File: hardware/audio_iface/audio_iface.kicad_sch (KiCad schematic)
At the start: 0 parts

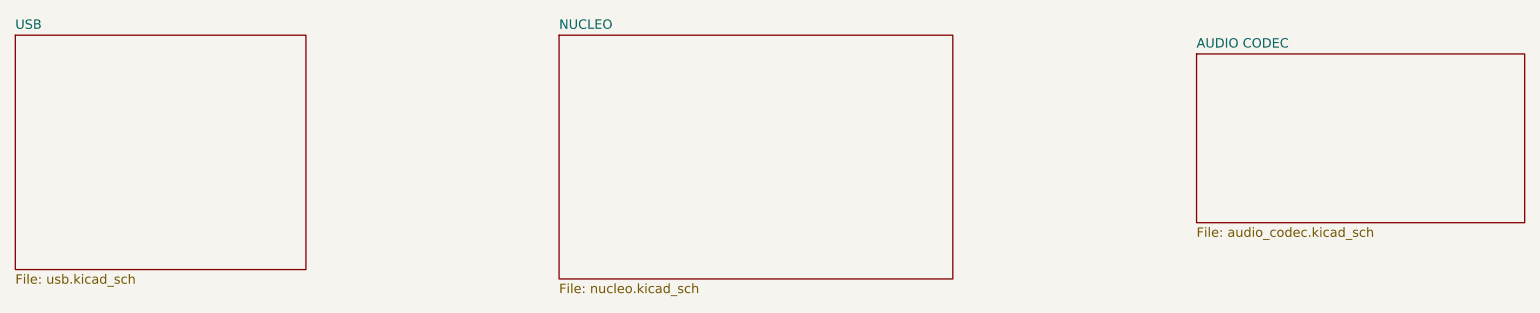
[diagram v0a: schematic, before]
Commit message: added some connections
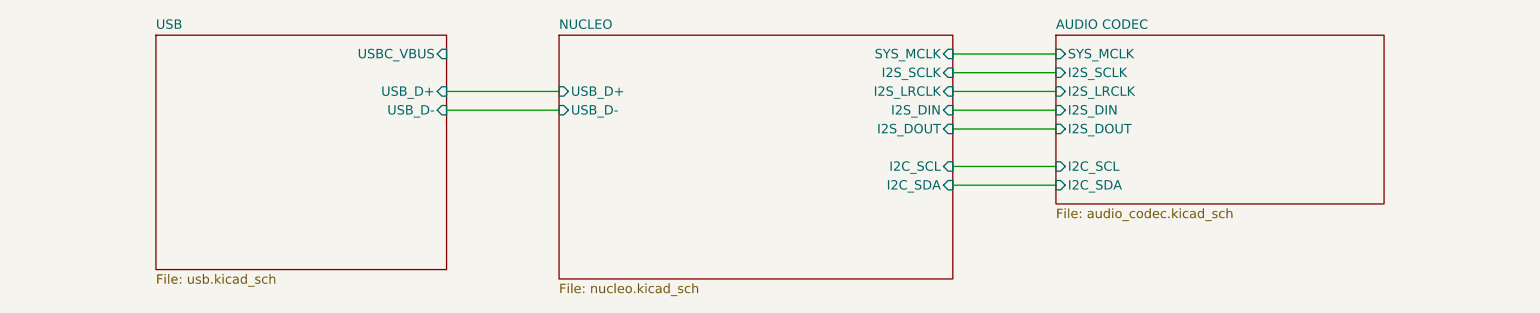
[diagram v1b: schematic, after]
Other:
- sheet AUDIO CODEC ports: added I2C_SCL, I2C_SDA, I2S_DIN, I2S_DOUT, I2S_LRCLK, I2S_SCLK, SYS_MCLK; removed none
- sheet NUCLEO ports: added I2C_SCL, I2C_SDA, I2S_DIN, I2S_DOUT, I2S_LRCLK, I2S_SCLK, SYS_MCLK, USB_D+, USB_D-; removed none
- sheet USB ports: added USBC_VBUS, USB_D+, USB_D-; removed none
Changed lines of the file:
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@@
 (kicad_sch (version 20230121) (generator eeschema)
   (paper "A4")
-  (sheet (at 193.04 59.69) (size 44.45 22.86) (fields_autoplaced)
+  (wire (pts (xy 160.02 62.23) (xy 173.99 62.23))
+    (stroke (width 0) (type default))
+  )
+  (wire (pts (xy 160.02 77.47) (xy 173.99 77.47))
+    (stroke (width 0) (type default))
+  )
+  (wire (pts (xy 160.02 64.77) (xy 173.99 64.77))
+    (stroke (width 0) (type default))
+  )
+  (wire (pts (xy 160.02 59.69) (xy 173.99 59.69))
+    (stroke (width 0) (type default))
+  )
+  (wire (pts (xy 91.44 67.31) (xy 106.68 67.31))
+    (stroke (width 0) (type default))
+  )
+  (wire (pts (xy 160.02 67.31) (xy 173.99 67.31))
+    (stroke (width 0) (type default))
+  )
+  (wire (pts (xy 160.02 69.85) (xy 173.99 69.85))
+    (stroke (width 0) (type default))
+  )
+  (wire (pts (xy 91.44 64.77) (xy 106.68 64.77))
+    (stroke (width 0) (type default))
+  )
+  (wire (pts (xy 160.02 74.93) (xy 173.99 74.93))
+    (stroke (width 0) (type default))
+  )
+  (sheet (at 173.99 57.15) (size 44.45 22.86) (fields_autoplaced)
     (stroke (width 0.1524) (type solid))
     (fill (color 0 0 0 0.0000))
-    (property "Sheetname" "AUDIO CODEC" (at 193.04 58.9784 0)
+    (property "Sheetname" "AUDIO CODEC" (at 173.99 56.4384 0)
       (effects (font (size 1.27 1.27)) (justify left bottom))
     )
-    (property "Sheetfile" "audio_codec.kicad_sch" (at 193.04 83.1346 0)
+    (property "Sheetfile" "audio_codec.kicad_sch" (at 173.99 80.5946 0)
       (effects (font (size 1.27 1.27)) (justify left top))
     )
-    (property "Field2" "" (at 193.04 59.69 0)
+    (property "Field2" "" (at 173.99 57.15 0)
       (effects (font (size 1.27 1.27)) hide)
+    )
+    (pin "I2S_LRCLK" input (at 173.99 64.77 180)
+      (effects (font (size 1.27 1.27)) (justify left))
+    )
+    (pin "I2S_DOUT" input (at 173.99 69.85 180)
+      (effects (font (size 1.27 1.27)) (justify left))
+    )
+    (pin "I2S_SCLK" input (at 173.99 62.23 180)
+      (effects (font (size 1.27 1.27)) (justify left))
+    )
+    (pin "I2S_DIN" input (at 173.99 67.31 180)
+      (effects (font (size 1.27 1.27)) (justify left))
+    )
+    (pin "SYS_MCLK" input (at 173.99 59.69 180)
+      (effects (font (size 1.27 1.27)) (justify left))
+    )
+    (pin "I2C_SDA" input (at 173.99 77.47 180)
+      (effects (font (size 1.27 1.27)) (justify left))
+    )
+    (pin "I2C_SCL" input (at 173.99 74.93 180)
+      (effects (font (size 1.27 1.27)) (justify left))
     )
     (instances
@@
       (effects (font (size 1.27 1.27)) hide)
     )
+    (pin "I2S_LRCLK" input (at 160.02 64.77 0)
+      (effects (font (size 1.27 1.27)) (justify right))
+    )
+    (pin "SYS_MCLK" input (at 160.02 59.69 0)
+      (effects (font (size 1.27 1.27)) (justify right))
+    )
+    (pin "I2S_DOUT" input (at 160.02 69.85 0)
+      (effects (font (size 1.27 1.27)) (justify right))
+    )
+    (pin "I2S_SCLK" input (at 160.02 62.23 0)
+      (effects (font (size 1.27 1.27)) (justify right))
+    )
+    (pin "I2S_DIN" input (at 160.02 67.31 0)
+      (effects (font (size 1.27 1.27)) (justify right))
+    )
+    (pin "I2C_SDA" input (at 160.02 77.47 0)
+      (effects (font (size 1.27 1.27)) (justify right))
+    )
+    (pin "USB_D+" input (at 106.68 64.77 180)
+      (effects (font (size 1.27 1.27)) (justify left))
+    )
+    (pin "USB_D-" input (at 106.68 67.31 180)
+      (effects (font (size 1.27 1.27)) (justify left))
+    )
+    (pin "I2C_SCL" input (at 160.02 74.93 0)
+      (effects (font (size 1.27 1.27)) (justify right))
+    )
     (instances
       (project "audio_iface"
@@
     )
   )
-  (sheet (at 33.02 57.15) (size 39.37 31.75) (fields_autoplaced)
+  (sheet (at 52.07 57.15) (size 39.37 31.75) (fields_autoplaced)
     (stroke (width 0.1524) (type solid))
     (fill (color 0 0 0 0.0000))
-    (property "Sheetname" "USB" (at 33.02 56.4384 0)
+    (property "Sheetname" "USB" (at 52.07 56.4384 0)
       (effects (font (size 1.27 1.27)) (justify left bottom))
     )
-    (property "Sheetfile" "usb.kicad_sch" (at 33.02 89.4846 0)
+    (property "Sheetfile" "usb.kicad_sch" (at 52.07 89.4846 0)
       (effects (font (size 1.27 1.27)) (justify left top))
     )
-    (property "Field2" "" (at 33.02 57.15 0)
+    (property "Field2" "" (at 52.07 57.15 0)
       (effects (font (size 1.27 1.27)) hide)
     )
+    (pin "USBC_VBUS" input (at 91.44 59.69 0)
+      (effects (font (size 1.27 1.27)) (justify right))
+    )
+    (pin "USB_D+" input (at 91.44 64.77 0)
+      (effects (font (size 1.27 1.27)) (justify right))
+    )
+    (pin "USB_D-" input (at 91.44 67.31 0)
+      (effects (font (size 1.27 1.27)) (justify right))
+    )
     (instances

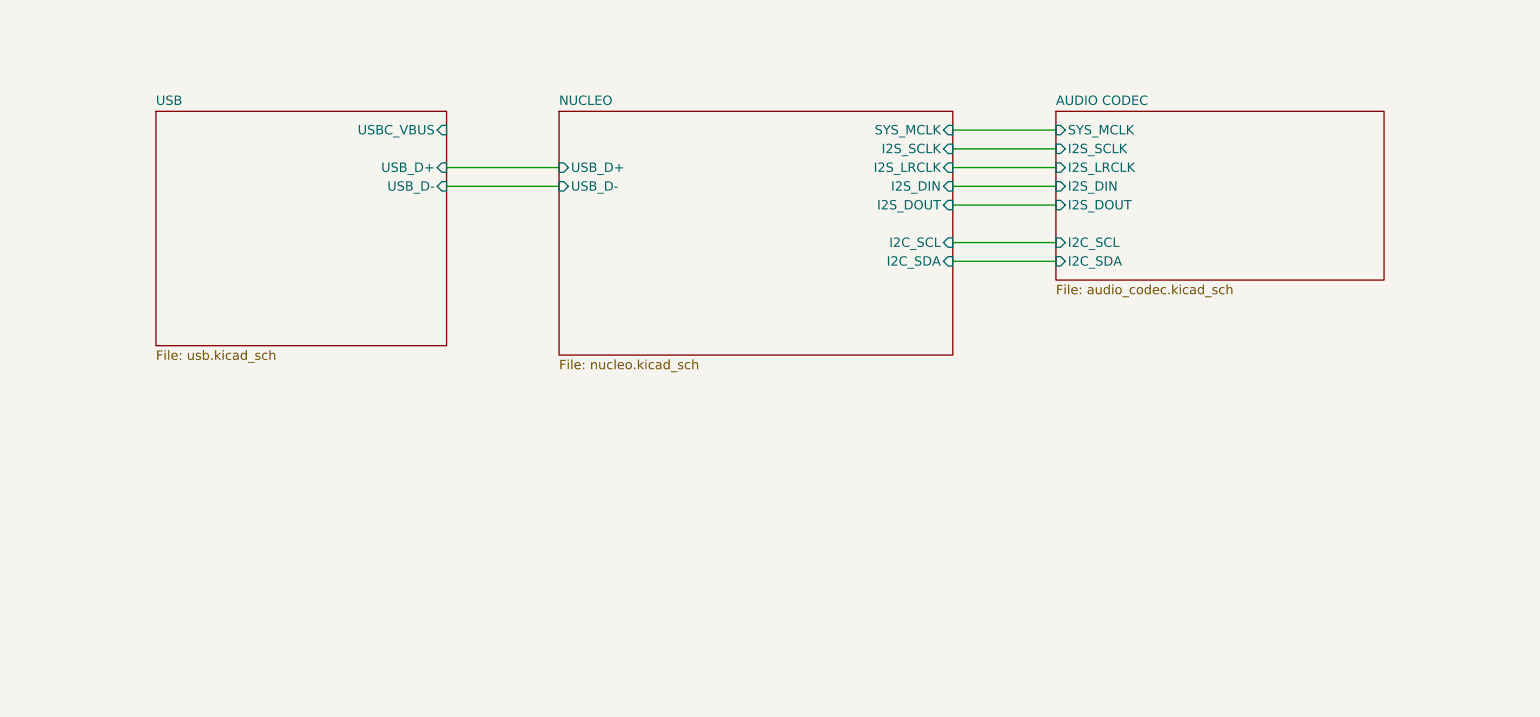
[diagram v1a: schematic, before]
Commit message: Added LEDs
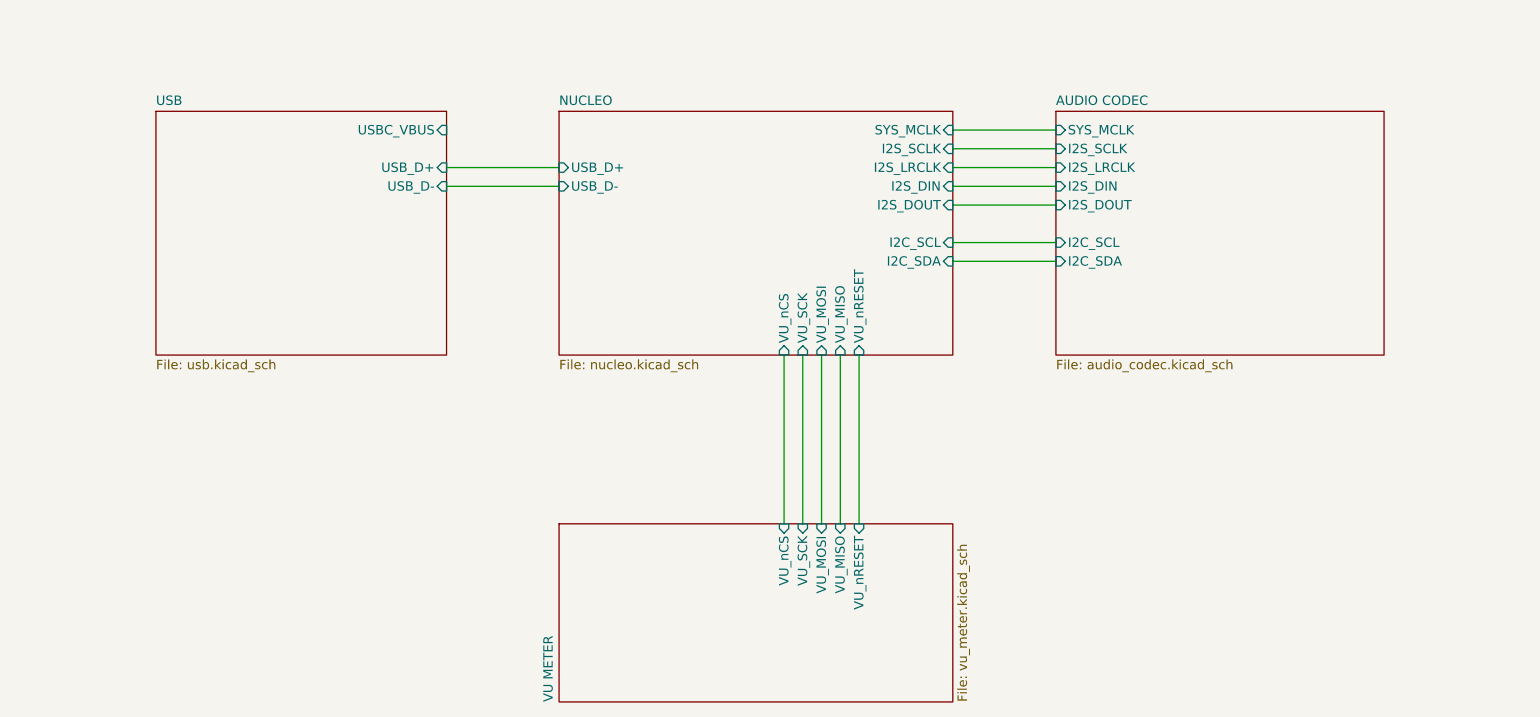
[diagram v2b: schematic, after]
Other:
- added sheet VU METER (vu_meter.kicad_sch)
- sheet NUCLEO ports: added VU_MISO, VU_MOSI, VU_SCK, VU_nCS, VU_nRESET; removed none
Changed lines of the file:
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@@
 (kicad_sch (version 20230121) (generator eeschema)
   (paper "A4")
+  (wire (pts (xy 137.16 90.17) (xy 137.16 113.03))
+    (stroke (width 0) (type default))
+  )
+  (wire (pts (xy 139.7 90.17) (xy 139.7 113.03))
+    (stroke (width 0) (type default))
+  )
   (wire (pts (xy 160.02 62.23) (xy 173.99 62.23))
     (stroke (width 0) (type default))
@@
   )
   (wire (pts (xy 160.02 59.69) (xy 173.99 59.69))
+    (stroke (width 0) (type default))
+  )
+  (wire (pts (xy 144.78 90.17) (xy 144.78 113.03))
     (stroke (width 0) (type default))
   )
@@
     (stroke (width 0) (type default))
   )
+  (wire (pts (xy 142.24 90.17) (xy 142.24 113.03))
+    (stroke (width 0) (type default))
+  )
   (wire (pts (xy 160.02 74.93) (xy 173.99 74.93))
     (stroke (width 0) (type default))
   )
-  (sheet (at 173.99 57.15) (size 44.45 22.86) (fields_autoplaced)
+  (wire (pts (xy 147.32 90.17) (xy 147.32 113.03))
+    (stroke (width 0) (type default))
+  )
+  (sheet (at 106.68 113.03) (size 53.34 24.13) (fields_autoplaced)
+    (stroke (width 0.1524) (type solid))
+    (fill (color 0 0 0 0.0000))
+    (property "Sheetname" "VU METER" (at 105.9684 137.16 90)
+      (effects (font (size 1.27 1.27)) (justify left bottom))
+    )
+    (property "Sheetfile" "vu_meter.kicad_sch" (at 160.6046 137.16 90)
+      (effects (font (size 1.27 1.27)) (justify left top))
+    )
+    (pin "VU_MISO" input (at 144.78 113.03 90)
+      (effects (font (size 1.27 1.27)) (justify right))
+    )
+    (pin "VU_nCS" input (at 137.16 113.03 90)
+      (effects (font (size 1.27 1.27)) (justify right))
+    )
+    (pin "VU_SCK" input (at 139.7 113.03 90)
+      (effects (font (size 1.27 1.27)) (justify right))
+    )
+    (pin "VU_MOSI" input (at 142.24 113.03 90)
+      (effects (font (size 1.27 1.27)) (justify right))
+    )
+    (pin "VU_nRESET" input (at 147.32 113.03 90)
+      (effects (font (size 1.27 1.27)) (justify right))
+    )
+    (instances
+      (project "audio_iface"
+        (path "/84adbf2e-65c7-4710-86f9-725cae0256c9" (page "5"))
+      )
+    )
+  )
+  (sheet (at 173.99 57.15) (size 44.45 33.02) (fields_autoplaced)
     (stroke (width 0.1524) (type solid))
     (fill (color 0 0 0 0.0000))
@@
       (effects (font (size 1.27 1.27)) (justify left bottom))
     )
-    (property "Sheetfile" "audio_codec.kicad_sch" (at 173.99 80.5946 0)
+    (property "Sheetfile" "audio_codec.kicad_sch" (at 173.99 90.7546 0)
       (effects (font (size 1.27 1.27)) (justify left top))
     )
@@
       (effects (font (size 1.27 1.27)) (justify right))
     )
+    (pin "VU_MOSI" input (at 142.24 90.17 270)
+      (effects (font (size 1.27 1.27)) (justify left))
+    )
+    (pin "VU_nCS" input (at 137.16 90.17 270)
+      (effects (font (size 1.27 1.27)) (justify left))
+    )
+    (pin "VU_MISO" input (at 144.78 90.17 270)
+      (effects (font (size 1.27 1.27)) (justify left))
+    )
+    (pin "VU_SCK" input (at 139.7 90.17 270)
+      (effects (font (size 1.27 1.27)) (justify left))
+    )
+    (pin "VU_nRESET" input (at 147.32 90.17 270)
+      (effects (font (size 1.27 1.27)) (justify left))
+    )
     (instances
       (project "audio_iface"
@@
     )
   )
-  (sheet (at 52.07 57.15) (size 39.37 31.75) (fields_autoplaced)
+  (sheet (at 52.07 57.15) (size 39.37 33.02) (fields_autoplaced)
     (stroke (width 0.1524) (type solid))
     (fill (color 0 0 0 0.0000))
@@
       (effects (font (size 1.27 1.27)) (justify left bottom))
     )
-    (property "Sheetfile" "usb.kicad_sch" (at 52.07 89.4846 0)
+    (property "Sheetfile" "usb.kicad_sch" (at 52.07 90.7546 0)
       (effects (font (size 1.27 1.27)) (justify left top))
     )

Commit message: schematic v1 done
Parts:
- added TP301 (x12): TestPoint, Connector_Pin:Pin_D1.1mm_L8.5mm_W2.5mm_FlatFork, symbol Connector:TestPoint
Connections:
- net AUDIO CODEC/I2C_SCL: now also TP301.1
- net AUDIO CODEC/I2C_SDA: now also TP301.1
- net AUDIO CODEC/I2S_DIN: now also TP301.1
- net AUDIO CODEC/I2S_DOUT: now also TP301.1
- net AUDIO CODEC/I2S_LRCLK: now also TP301.1
- net AUDIO CODEC/I2S_SCLK: now also TP301.1
- net AUDIO CODEC/SYS_MCLK: now also TP301.1
- net NUCLEO/VU_MISO: now also TP301.1
- net NUCLEO/VU_MOSI: now also TP301.1
- net NUCLEO/VU_SCK: now also TP301.1
- net NUCLEO/VU_nCS: now also TP301.1
- net NUCLEO/VU_nRESET: now also TP301.1

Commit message: crude placement
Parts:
- TP301: value TestPoint -> SDA
- TP301: value TestPoint -> MCLK
- TP301: value TestPoint -> SCL
- TP301: value TestPoint -> DIN
- TP301: value TestPoint -> MISO
- TP301: value TestPoint -> nCS
- TP301: value TestPoint -> MOSI
- TP301: value TestPoint -> SCK
- TP301: value TestPoint -> LRCLK
- TP301: value TestPoint -> nRESET
- TP301: value TestPoint -> DOUT
- TP301: value TestPoint -> SCLK
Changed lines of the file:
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@@
       (effects (font (size 1.27 1.27)) (justify left))
     )
-    (property "Value" "TestPoint" (at 180.34 53.848 0)
+    (property "Value" "SDA" (at 180.34 53.848 0)
       (effects (font (size 1.27 1.27)) (justify left) hide)
     )
@@
       (effects (font (size 1.27 1.27)) (justify left))
     )
-    (property "Value" "TestPoint" (at 165.1 53.848 0)
+    (property "Value" "MCLK" (at 165.1 53.848 0)
       (effects (font (size 1.27 1.27)) (justify left) hide)
     )
@@
       (effects (font (size 1.27 1.27)) (justify left))
     )
-    (property "Value" "TestPoint" (at 177.8 53.848 0)
+    (property "Value" "SCL" (at 177.8 53.848 0)
       (effects (font (size 1.27 1.27)) (justify left) hide)
     )
@@
       (effects (font (size 1.27 1.27)) (justify left))
     )
-    (property "Value" "TestPoint" (at 172.72 53.848 0)
+    (property "Value" "DIN" (at 172.72 53.848 0)
       (effects (font (size 1.27 1.27)) (justify left) hide)
     )
@@
       (effects (font (size 1.27 1.27)) (justify left))
     )
-    (property "Value" "TestPoint" (at 151.892 100.33 0)
+    (property "Value" "MISO" (at 151.892 100.33 0)
       (effects (font (size 1.27 1.27)) (justify left) hide)
     )
@@
       (effects (font (size 1.27 1.27)) (justify left))
     )
-    (property "Value" "TestPoint" (at 151.892 107.95 0)
+    (property "Value" "nCS" (at 151.892 107.95 0)
       (effects (font (size 1.27 1.27)) (justify left) hide)
     )
@@
       (effects (font (size 1.27 1.27)) (justify left))
     )
-    (property "Value" "TestPoint" (at 151.892 102.87 0)
+    (property "Value" "MOSI" (at 151.892 102.87 0)
       (effects (font (size 1.27 1.27)) (justify left) hide)
     )
@@
       (effects (font (size 1.27 1.27)) (justify left))
     )
-    (property "Value" "TestPoint" (at 151.892 105.41 0)
+    (property "Value" "SCK" (at 151.892 105.41 0)
       (effects (font (size 1.27 1.27)) (justify left) hide)
     )
@@
       (effects (font (size 1.27 1.27)) (justify left))
     )
-    (property "Value" "TestPoint" (at 170.18 53.848 0)
+    (property "Value" "LRCLK" (at 170.18 53.848 0)
       (effects (font (size 1.27 1.27)) (justify left) hide)
     )
@@
       (effects (font (size 1.27 1.27)) (justify left))
     )
-    (property "Value" "TestPoint" (at 151.892 97.79 0)
+    (property "Value" "nRESET" (at 151.892 97.79 0)
       (effects (font (size 1.27 1.27)) (justify left) hide)
     )
@@
       (effects (font (size 1.27 1.27)) (justify left))
     )
-    (property "Value" "TestPoint" (at 175.26 53.848 0)
+    (property "Value" "DOUT" (at 175.26 53.848 0)
       (effects (font (size 1.27 1.27)) (justify left) hide)
     )
@@
       (effects (font (size 1.27 1.27)) (justify left))
     )
-    (property "Value" "TestPoint" (at 167.64 53.848 0)
-      (effects (font (size 1.27 1.27)) (justify left) hide)
-    )
+    (property "Value" "SCLK" (at 167.64 53.848 0)
+      (effects (font (size 1.27 1.27)) (justify left) hide)
+    )

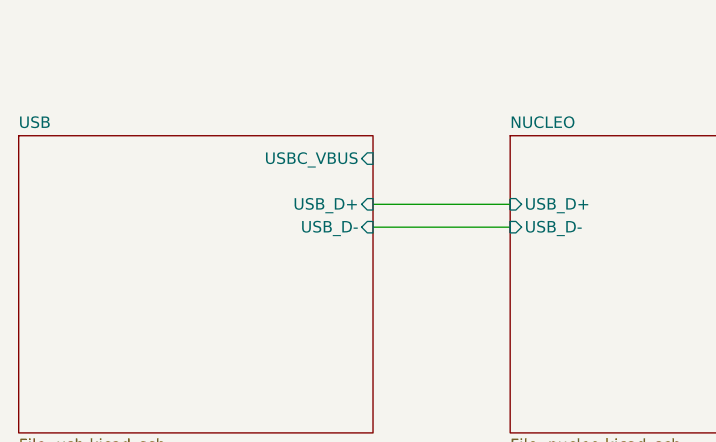
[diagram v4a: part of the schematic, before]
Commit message: add logo
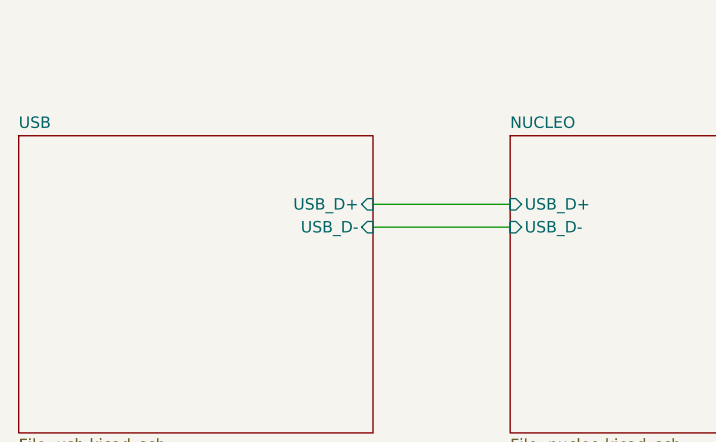
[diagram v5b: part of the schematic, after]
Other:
- sheet USB ports: added none; removed USBC_VBUS
